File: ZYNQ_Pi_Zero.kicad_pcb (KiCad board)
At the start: 4 copper layers, 35 parts, among them Q501 2N7002, Q502 2N7002, Q503 2N7002, U101 xc7z010clg400, U201 MT41K256M16TW-107_P, U301 W25Q256FVEI, U501 TPD4E05U06DQA, U502 TPD4E05U06DQA

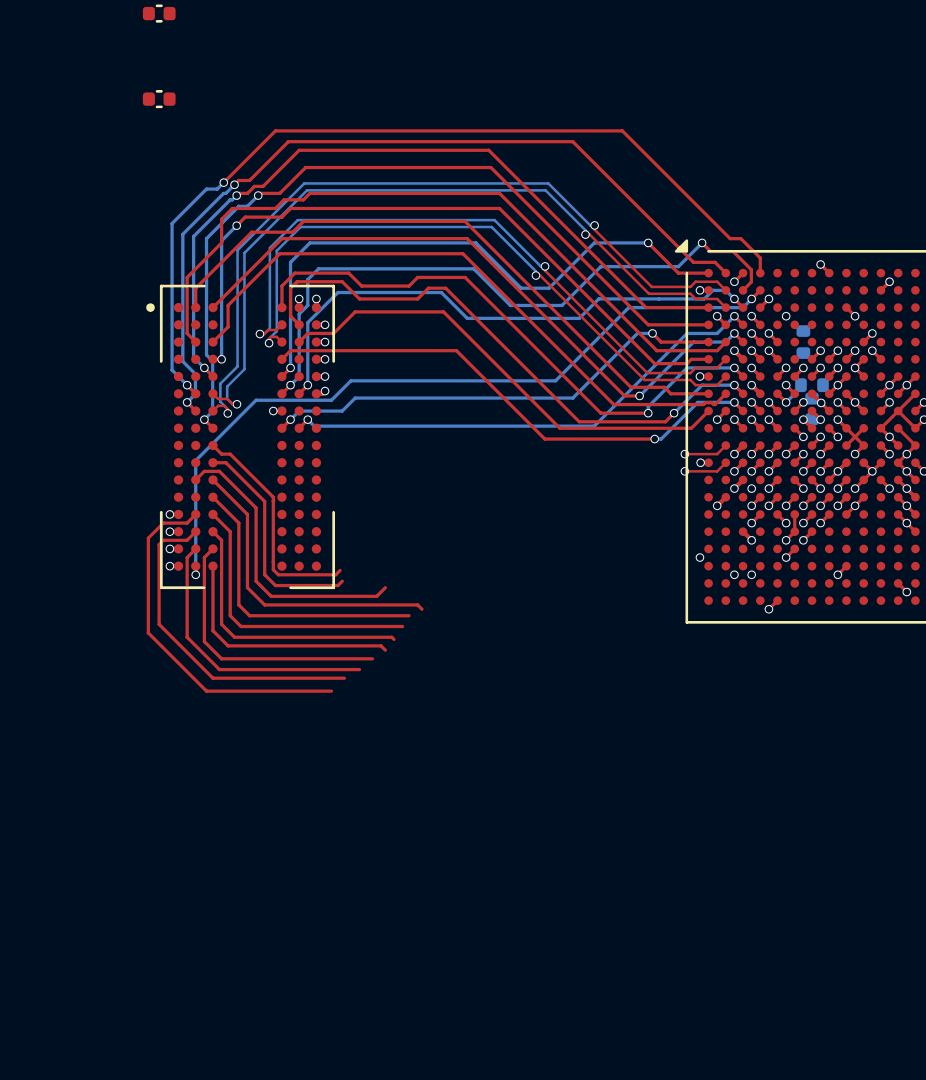
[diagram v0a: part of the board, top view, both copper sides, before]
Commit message: feat: add serial res
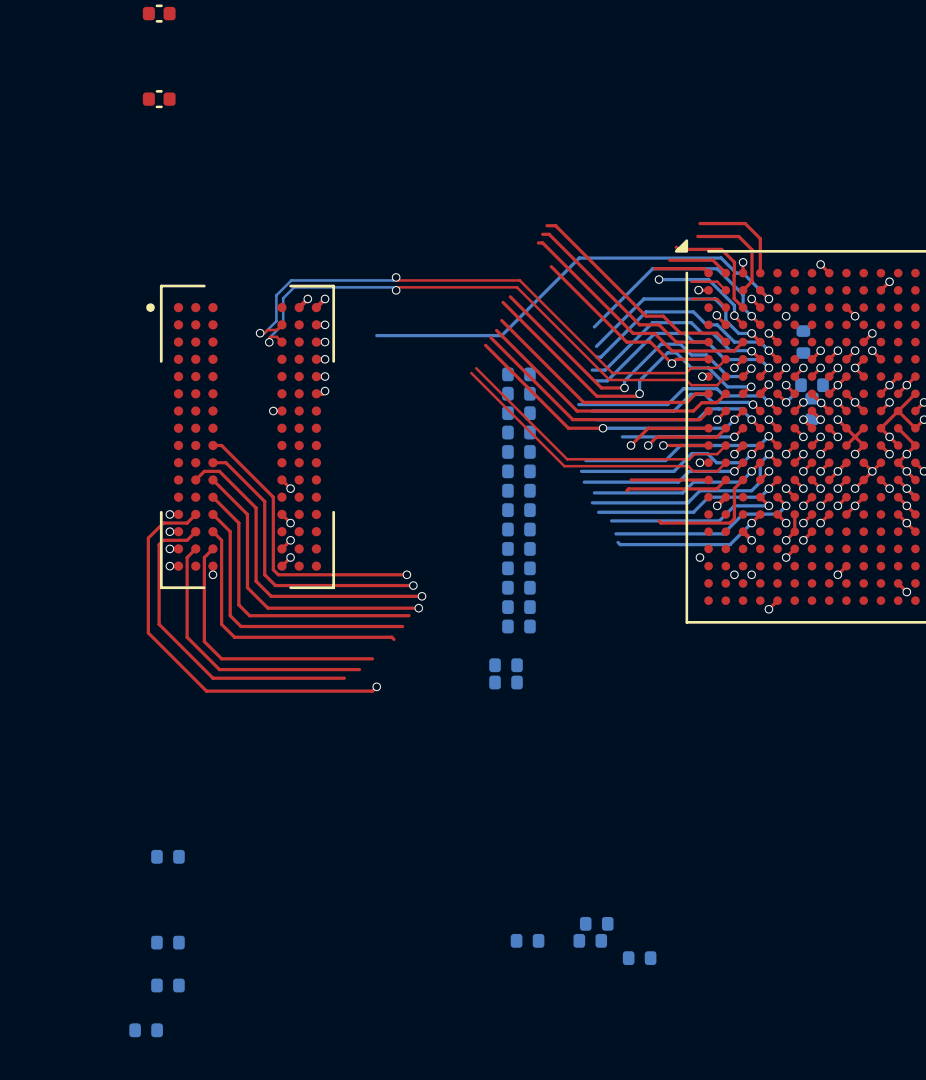
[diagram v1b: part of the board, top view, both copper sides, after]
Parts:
- added R207: 10R, Resistor_SMD:R_0402_1005Metric, B.Cu at (136.2, 122.6)
- added R208: 10R, Resistor_SMD:R_0402_1005Metric, B.Cu at (135.9, 123.4)
- added R209: 10R, Resistor_SMD:R_0402_1005Metric, B.Cu at (132.6, 107.0)
- added R210: 10R, Resistor_SMD:R_0402_1005Metric, B.Cu at (132.6, 104.3)
- added R211: 10R, Resistor_SMD:R_0402_1005Metric, B.Cu at (132.6, 107.9)
- added R212: 10R, Resistor_SMD:R_0402_1005Metric, B.Cu at (138.2, 124.2)
- added R213: 10R, Resistor_SMD:R_0402_1005Metric, B.Cu at (132.6, 106.1)
- added R214: 10R, Resistor_SMD:R_0402_1005Metric, B.Cu at (132.6, 103.4)
- added R215: 10R, Resistor_SMD:R_0402_1005Metric, B.Cu at (133.0, 123.4)
- added R216: 10R, Resistor_SMD:R_0402_1005Metric, B.Cu at (132.6, 102.5)
- added R217: 10R, Resistor_SMD:R_0402_1005Metric, B.Cu at (132.6, 98.9)
- added R218: 10R, Resistor_SMD:R_0402_1005Metric, B.Cu at (132.6, 100.7)
- added R219: 10R, Resistor_SMD:R_0402_1005Metric, B.Cu at (132.6, 98.0)
- added R220: 10R, Resistor_SMD:R_0402_1005Metric, B.Cu at (132.6, 97.1)
- added R221: 10R, Resistor_SMD:R_0402_1005Metric, B.Cu at (132.6, 99.8)
- added R222: 10R, Resistor_SMD:R_0402_1005Metric, B.Cu at (132.6, 105.2)
- added R223: 10R, Resistor_SMD:R_0402_1005Metric, B.Cu at (116.3, 119.5)
- added R224: 10R, Resistor_SMD:R_0402_1005Metric, B.Cu at (132.6, 101.6)
- added R225: 10R, Resistor_SMD:R_0402_1005Metric, B.Cu at (116.3, 123.5)
- added R226: 10R, Resistor_SMD:R_0402_1005Metric, B.Cu at (116.3, 125.5)
- added R227: 10R, Resistor_SMD:R_0402_1005Metric, B.Cu at (115.3, 127.5)
- added R229: 10R, Resistor_SMD:R_0402_1005Metric, B.Cu at (132.0, 110.6)
- added R230: 10R, Resistor_SMD:R_0402_1005Metric, B.Cu at (132.6, 108.8)
- added R231: 10R, Resistor_SMD:R_0402_1005Metric, B.Cu at (132.0, 111.4)
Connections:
- U101 pad D4: /DDR3/DDR_A13 -> /DDR3/PS_DDR_A13
- U101 pad E4: /DDR3/DDR_A12 -> /DDR3/PS_DDR_A12
- U101 pad F4: /DDR3/DDR_A14 -> /DDR3/PS_DDR_A14
- U101 pad F5: /DDR3/DDR_A10 -> /DDR3/PS_DDR_A10
- U101 pad G4: /DDR3/DDR_A11 -> /DDR3/PS_DDR_A11
- U101 pad J4: /DDR3/DDR_A9 -> /DDR3/PS_DDR_A9
- U101 pad J5: /DDR3/DDR_BA2 -> /DDR3/PS_DDR_BA2
- U101 pad K1: /DDR3/DDR_A8 -> /DDR3/PS_DDR_A8
- U101 pad K2: /DDR3/DDR_A1 -> /DDR3/PS_DDR_A1
- U101 pad K3: /DDR3/DDR_A3 -> /DDR3/PS_DDR_A3
- U101 pad K4: /DDR3/DDR_A7 -> /DDR3/PS_DDR_A7
- U101 pad L1: /DDR3/DDR_A5 -> /DDR3/PS_DDR_A5
- U101 pad L4: /DDR3/DDR_A6 -> /DDR3/PS_DDR_A6
- U101 pad L5: /DDR3/DDR_BA0 -> /DDR3/PS_DDR_BA0
- U101 pad M3: /DDR3/DDR_A2 -> /DDR3/PS_DDR_A2
- U101 pad M4: /DDR3/DDR_A4 -> /DDR3/PS_DDR_A4
- U101 pad M5: /DDR3/DDR_~{WE} -> /DDR3/PS_DDR_~{WE}
- U101 pad N1: /DDR3/DDR_~{CS} -> /DDR3/PS_DDR_~{CS}
- U101 pad N2: /DDR3/DDR_A0 -> /DDR3/PS_DDR_A0
- U101 pad N3: /DDR3/DDR_CKE -> /DDR3/PS_DDR_CKE
- U101 pad N5: /DDR3/DDR_ODT -> /DDR3/PS_DDR_ODT
- U101 pad P4: /DDR3/DDR_~{RAS} -> /DDR3/PS_DDR_~{RAS}
- U101 pad P5: /DDR3/DDR_~{CAS} -> /DDR3/PS_DDR_~{CAS}
- U101 pad R4: /DDR3/DDR_BA1 -> /DDR3/PS_DDR_BA1
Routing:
- net /DDR3/DDR_D5: track 36.9 -> 0.00 mm, vias 2 -> 0
- net /DDR3/DDR_D3: track 40.6 -> 4.69 mm, vias 2 -> 0
- net /DDR3/DDR_D2: track 38.3 -> 2.85 mm, vias 2 -> 0
- net /DDR3/DDR_D6: track 35.5 -> 0.00 mm, vias 2 -> 0
- net /DDR3/DDR_DQS0_N: track 35.4 -> 1.77 mm, vias 2 -> 0
- net /DDR3/DDR_DQS0_P: track 34.9 -> 1.77 mm, vias 2 -> 0
- net /DDR3/DDR_D1: track 30.1 -> 4.83 mm, vias 2 -> 0
- net /DDR3/DDR_DM0: track 27.6 -> 2.58 mm, vias 2 -> 0
- net /DDR3/DDR_D8: track 33.6 -> 10.5 mm
- net /DDR3/DDR_DM1: track 32.2 -> 9.25 mm, vias 2 -> 1
- net /DDR3/DDR_D0: track 25.6 -> 5.27 mm, vias 2 -> 0
- net /DDR3/DDR_D9: track 30.3 -> 11.7 mm, vias 2 -> 0
- net /DDR3/DDR_D4: track 23.2 -> 5.06 mm
- net /DDR3/DDR_D14: track 29.3 -> 11.3 mm
- net /DDR3/DDR_D13: track 29.3 -> 12.5 mm
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
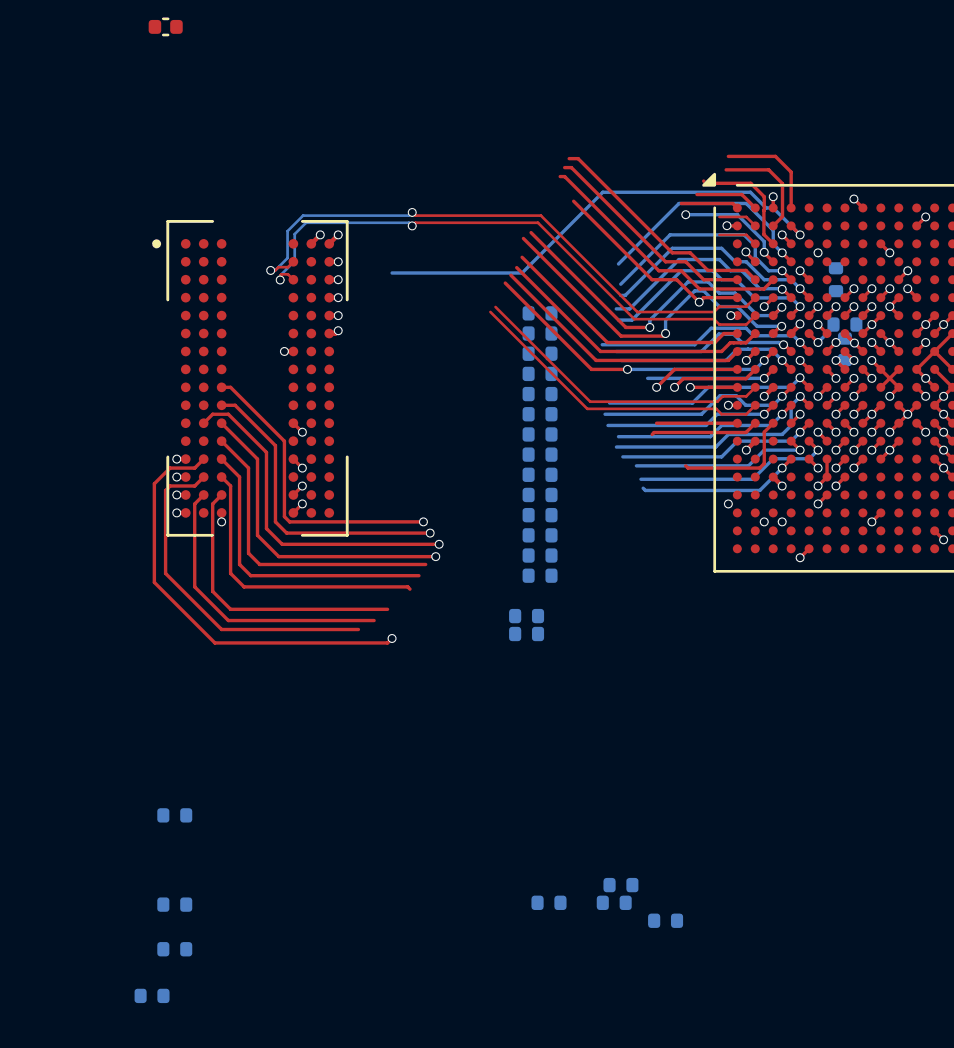
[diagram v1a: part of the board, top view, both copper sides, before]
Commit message: feat: finish basic ddr3 routing
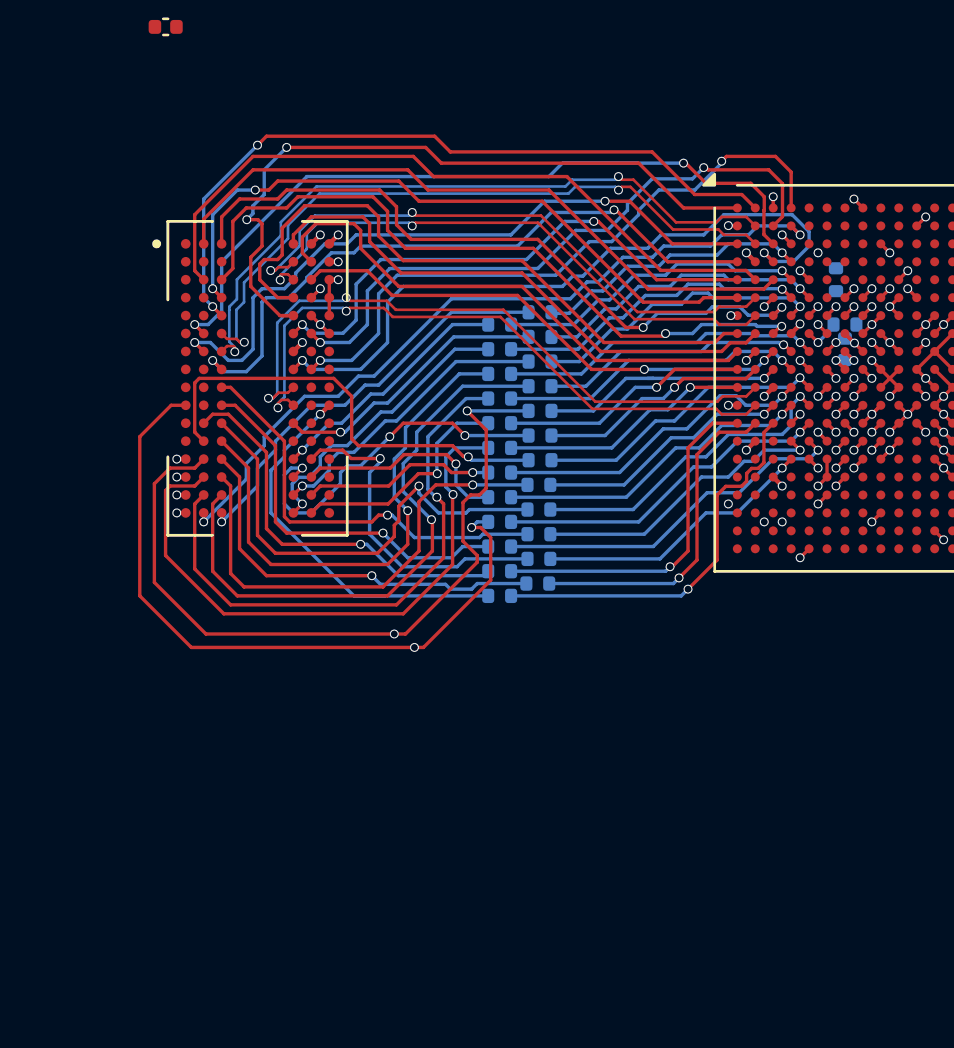
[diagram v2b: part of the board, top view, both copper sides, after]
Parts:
- moved R227 24.5 mm to (130.8, 108.6)
- moved R212 22.4 mm to (130.8, 103.1)
- moved R225 21.6 mm to (130.8, 107.5)
- moved R215 21.5 mm to (130.8, 102.0)
- moved R226 21.4 mm to (130.8, 109.7)
- moved R208 21.1 mm to (132.6, 102.5)
- moved R223 19.9 mm to (132.6, 108.0)
- moved R207 14.0 mm to (132.5, 109.2)
- moved R231 4.48 mm to (132.6, 107.0)
- moved R229 4.37 mm to (130.8, 106.4)
- moved R211 3.16 mm to (130.8, 105.3)
- moved R214 3.08 mm to (130.8, 100.9)
- moved R230 2.95 mm to (132.6, 105.8)
- moved R210 2.85 mm to (132.6, 101.5)
- moved R213 2.62 mm to (130.8, 104.2)
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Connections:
- U201 pad A2: /DDR3/DDR_D14 -> /DDR3/DDR_D9
- U201 pad A3: /DDR3/DDR_D9 -> /DDR3/DDR_D10
- U201 pad A7: /DDR3/DDR_D10 -> /DDR3/DDR_D13
- U201 pad B8: /DDR3/DDR_D11 -> /DDR3/DDR_D15
- U201 pad C3: /DDR3/DDR_D13 -> /DDR3/DDR_D11
- U201 pad C8: /DDR3/DDR_D15 -> /DDR3/DDR_D12
- U201 pad D7: /DDR3/DDR_D12 -> /DDR3/DDR_D14
- U201 pad E3: /DDR3/DDR_D6 -> /DDR3/DDR_D2
- U201 pad F2: /DDR3/DDR_D3 -> /DDR3/DDR_D0
- U201 pad F7: /DDR3/DDR_D1 -> /DDR3/DDR_D7
- U201 pad F8: /DDR3/DDR_D0 -> /DDR3/DDR_D1
- U201 pad G2: /DDR3/DDR_D2 -> /DDR3/DDR_D6
- U201 pad H7: /DDR3/DDR_D7 -> /DDR3/DDR_D4
- U201 pad H8: /DDR3/DDR_D4 -> /DDR3/DDR_D3
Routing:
- net /DDR3/DDR_ODT: track 0.00 -> 31.4 mm, vias 0 -> 2
- net /DDR3/DDR_D6: track 0.00 -> 30.3 mm, vias 0 -> 2
- net /DDR3/DDR_D2: track 2.85 -> 32.6 mm, vias 0 -> 2
- net /DDR3/DDR_D5: track 0.00 -> 29.6 mm, vias 0 -> 2
- net /DDR3/DDR_DM0: track 2.58 -> 31.9 mm, vias 0 -> 2
- net /DDR3/DDR_DQS0_N: track 1.77 -> 30.9 mm, vias 0 -> 2
- net /DDR3/DDR_DQS0_P: track 1.77 -> 30.3 mm, vias 0 -> 2
- net /DDR3/DDR_D0: track 5.27 -> 33.1 mm, vias 0 -> 2
- net /DDR3/DDR_D4: track 5.06 -> 31.2 mm
- net /DDR3/DDR_D3: track 4.69 -> 28.4 mm, vias 0 -> 2
- net /DDR3/DDR_D1: track 4.83 -> 27.8 mm, vias 0 -> 2
- net /DDR3/DDR_DM1: track 9.25 -> 30.2 mm, vias 1 -> 2
- net /DDR3/DDR_D8: track 10.5 -> 31.4 mm
- net /DDR3/DDR_BA0: track 0.00 -> 20.4 mm, vias 0 -> 1
- net /DDR3/DDR_A13: track 0.40 -> 18.7 mm
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
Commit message: feat: continue routing ddr
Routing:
- net /DDR3/DDR_ODT: track 31.4 -> 27.5 mm
- net /DDR3/DDR_A3: track 34.5 -> 32.3 mm
- net /DDR3/DDR_A2: track 21.1 -> 19.9 mm
- net /DDR3/DDR_A9: track 26.6 -> 25.5 mm
- net /DDR3/DDR_A5: track 26.6 -> 25.6 mm
- net /DDR3/DDR_A7: track 25.2 -> 24.2 mm
- net /DDR3/DDR_DM0: track 31.9 -> 31.0 mm
- net /DDR3/DDR_D10: track 31.4 -> 30.9 mm
- net /DDR3/DDR_BA2: track 23.2 -> 22.7 mm
